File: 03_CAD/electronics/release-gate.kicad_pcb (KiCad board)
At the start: 2 copper layers, 180 x 140 mm, 99 parts, among them J1 PWR_IN, J2 ACT_OUT, J3 SAFETY_IN, J4 PRELOAD_OUT, J5 HOME, J6 MODE_MAG, J7 ESTOP, J8 KEY, J9 STATUS, M1 AO3400A, M2 AO3400A, U1 74HC21, U2 74HC123, U3 74HC74, U4 74HC11, U5 74HC14, U6 74HC08

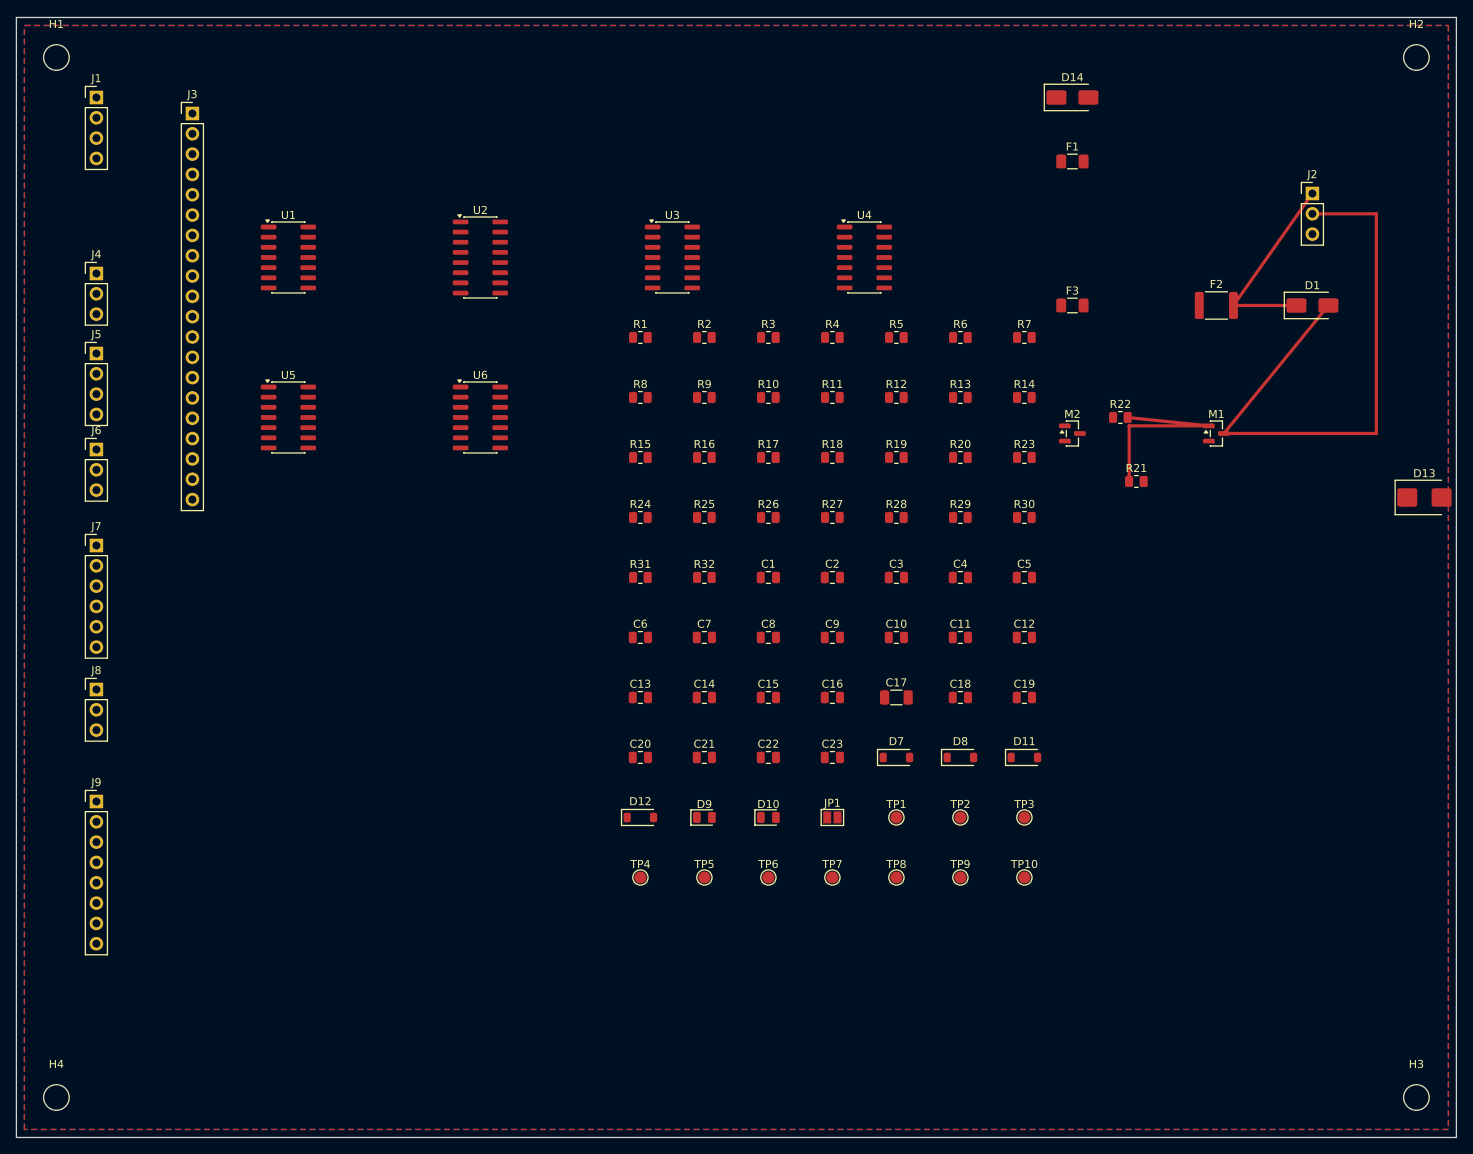
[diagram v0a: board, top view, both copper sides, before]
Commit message: 释放门控板自动布线，以及最终全量复验
自动布线
- 用 Freerouting 2.4.1 把板子布通：未连接项从 151 降到 23
- 管线建立在命令行工具上，不依赖那个挂掉的 KiCad MCP：
  pcbnew 导出 Specctra DSN、freerouting 命令行布线、pcbnew 回导 SES、pcbnew 重灌铜箔
- Freerouting 的无界面开关是 --gui.enabled=false。缺了它会试图拉 GUI，在无显示环境里挂死
- 重灌铜箔这一步不能省。省掉的话铜箔没避让新走线，DRC 会把 511 处报成短路，
  实测是 733 条违规；重灌后降到 31 条
- 铜箔焊盘连接由热焊盘改为实心，消掉了 11 条 starved_thermal

残留问题，已写进电子侧 README 第 14 节
- 线宽 19 条：DSN 与工程 netclass 都写 0.2 毫米，Freerouting 实际用了 0.15 毫米
- 未连接 23 条：Freerouting 自报只有 2 条布不通，其余应为重灌后不再靠铺铜连接的
- 丝印重叠 1 条

验证记录同步进 README，把自动布线前后的 DRC 数字分开列出，避免把两者混为一谈

最终全量复验
- 固件两环境构建 SUCCESS
- 算法参考实现 58 项、工具链 38 项、数值仿真 27 项，全通过
- CAD 五级几何自检全部跑通
- KiCad 原理图 ERC 0 error 0 warning
- 全库无破折号与禁用表述
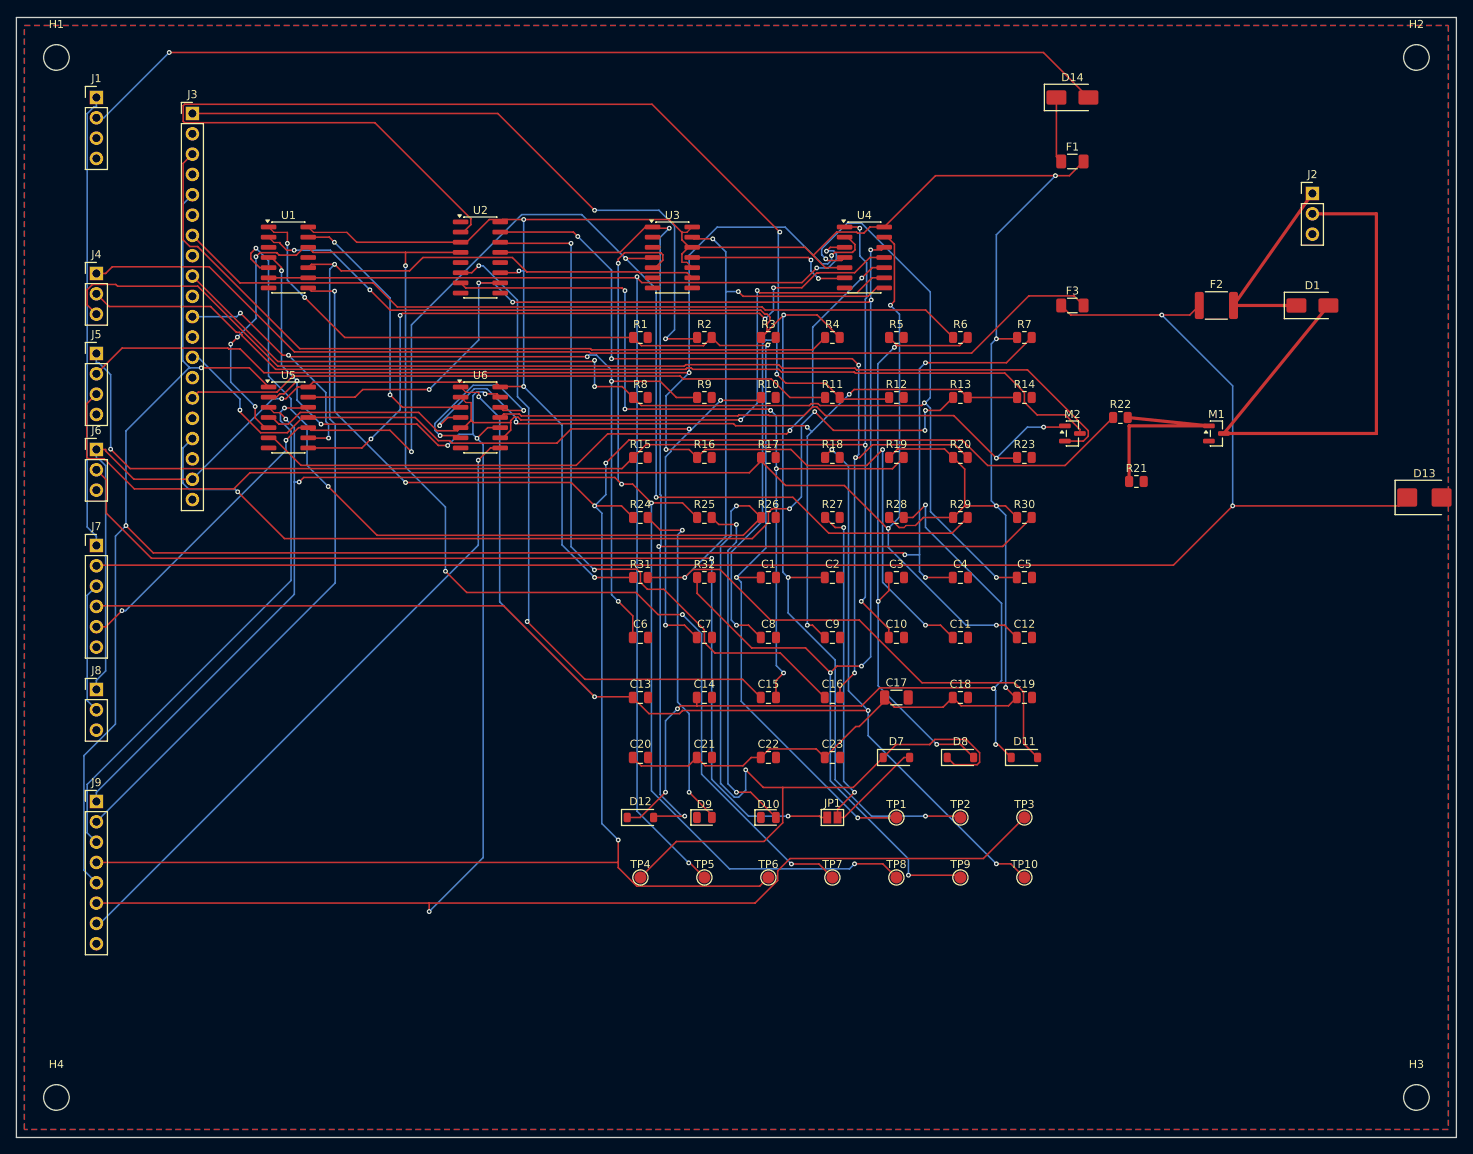
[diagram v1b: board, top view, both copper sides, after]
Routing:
- net +3V3: track 0.00 -> 427.1 mm, vias 0 -> 9
- net Q2_OUT: track 0.00 -> 267.5 mm, vias 0 -> 5
- net MECH_RECOVERED_RAW: track 0.00 -> 250.0 mm, vias 0 -> 5
- net MECH_RECOVERED_N: track 0.00 -> 246.2 mm, vias 0 -> 7
- net FAULT_LATCH: track 0.00 -> 222.2 mm, vias 0 -> 6
- net MASTER_ENABLE_RAW: track 0.00 -> 214.7 mm, vias 0 -> 5
- net V_ACT_SW: track 0.00 -> 213.2 mm, vias 0 -> 2
- net POCKET_OR_MODE_A: track 0.00 -> 205.4 mm, vias 0 -> 4
- net MCU_RELEASE_CMD: track 0.00 -> 202.7 mm, vias 0 -> 3
- net HOME_AND: track 0.00 -> 201.6 mm, vias 0 -> 8
- net TILT_HOME: track 0.00 -> 187.4 mm, vias 0 -> 5
- net FAULT_SET_N: track 0.00 -> 178.8 mm, vias 0 -> 5
- net MAG_HOME: track 0.00 -> 177.1 mm, vias 0 -> 3
- net RELEASE_PULSE: track 0.00 -> 167.9 mm, vias 0 -> 8
- net ARM_CMD: track 0.00 -> 165.4 mm, vias 0 -> 5
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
